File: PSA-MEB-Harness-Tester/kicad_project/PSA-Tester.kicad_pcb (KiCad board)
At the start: 4 copper layers, 100 x 100 mm, 41 parts, among them J11 TYPE-C-31-M-04, M1 MountingHole_3.2mm_M3_Pad_Via, M2 MountingHole_3.2mm_M3_Pad_Via, M3 MountingHole_3.2mm_M3_Pad_Via, M4 MountingHole_3.2mm_M3_Pad_Via, SW1 B3FS-1010P, SW2 B3FS-1010P, SW3 B3FS-1010P, U1 MCP23017T-E/SO, U10 ESP32-C3-OLED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

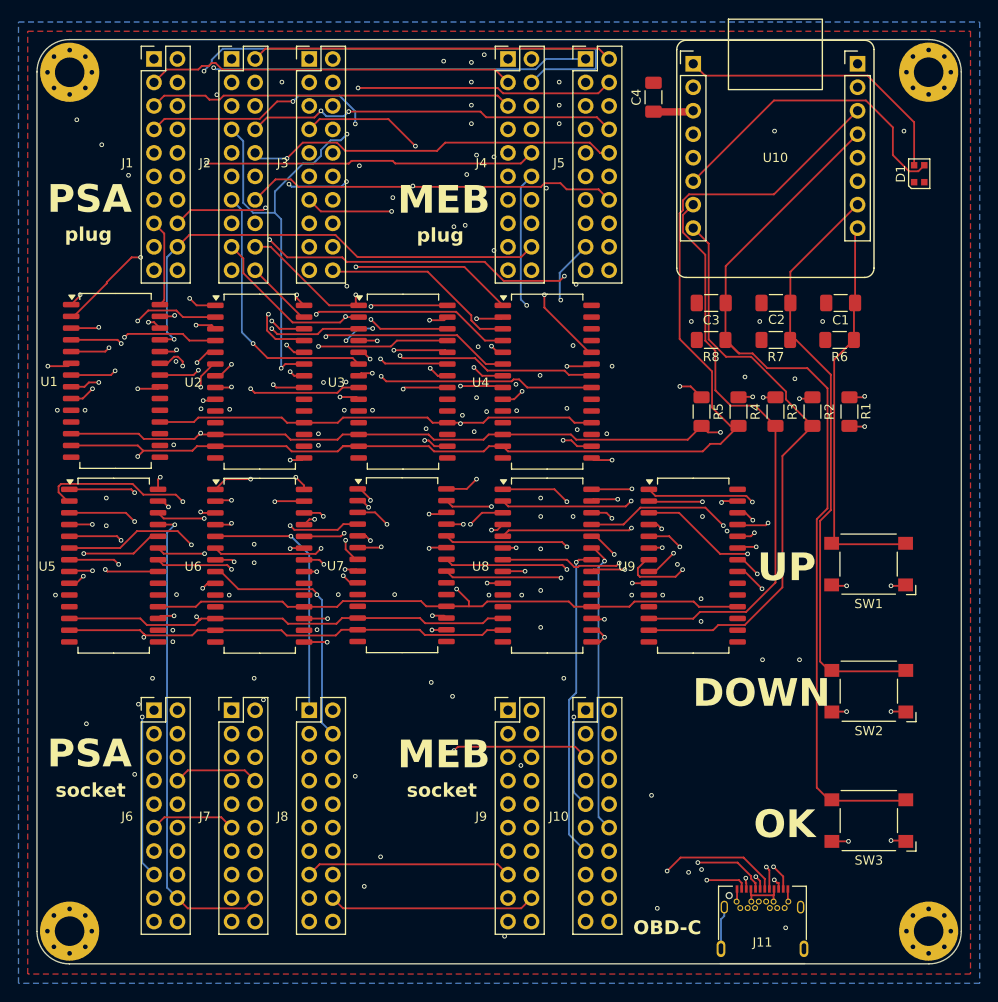
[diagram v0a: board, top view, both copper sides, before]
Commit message: fix PSA-Tester swapped pin headers
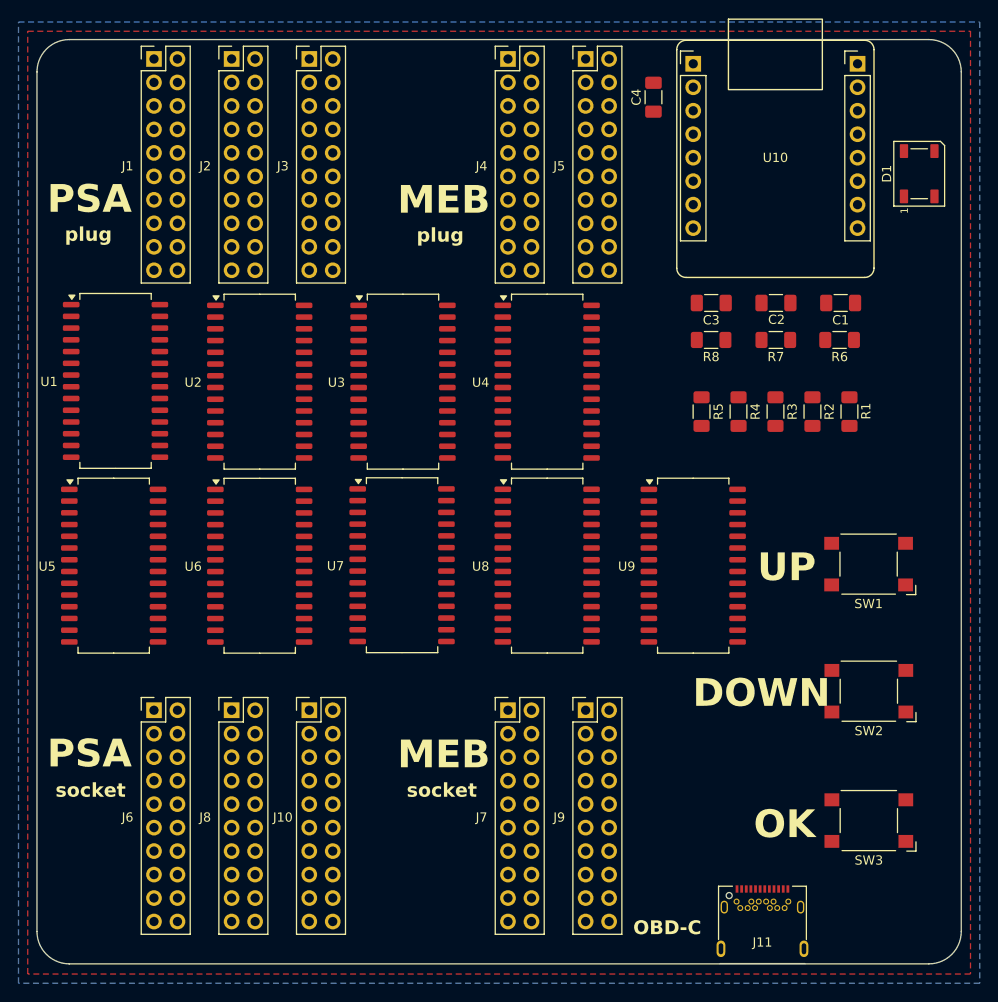
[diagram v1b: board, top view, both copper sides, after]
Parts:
- removed M1, M2, M3, M4: MountingHole_3.2mm_M3_Pad_Via, MountingHole:MountingHole_3.2mm_M3_Pad_Via
- D1: value XL-0807RGBC-WS2812B -> WS2812; footprint 0_tester:LED_WS2812B-2020_PLCC4_2.0x2.0mm -> LED_SMD:LED_WS2812B_PLCC4_5.0x5.0mm_P3.2mm
- J1, J10, J2, J3, J4, J5, J6, J7, J8, J9: footprint Connector_PinHeader_2.54mm:PinHeader_2x10_P2.54mm_Vertical -> 0_tester:PinHeader_2x10_P2.54mm_Vertical
- moved J10 29.9 mm to (68.5, 115.5)
- moved J7 29.9 mm to (90.0, 115.5)
- moved J9 8.40 mm to (98.4, 115.5)
- moved J8 8.40 mm to (60.1, 115.5)
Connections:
- J1 pad 11: 20 -> 11
- J1 pad 12: 19 -> 12
- J1 pad 13: 18 -> 13
- J1 pad 14: 17 -> 14
- J1 pad 15: 16 -> 15
- J1 pad 16: 15 -> 16
- J1 pad 17: 14 -> 17
- J1 pad 18: 13 -> 18
- J1 pad 19: 12 -> 19
- J1 pad 20: 11 -> 20
- J10 pad 11: 60a -> 51a
- J10 pad 12: 59a -> 52a
- J10 pad 13: 58a -> 53a
- J10 pad 14: 57a -> 54a
- J10 pad 15: 56a -> 55a
- J10 pad 16: 55a -> 56a
- J10 pad 17: 54a -> 57a
- J10 pad 18: 53a -> 58a
- J10 pad 19: 52a -> 59a
- J10 pad 20: 51a -> 60a
- J2 pad 11: 40 -> 31
- J2 pad 12: 39 -> 32
- J2 pad 13: 38 -> 33
- J2 pad 14: 37 -> 34
- J2 pad 15: 36 -> 35
- J2 pad 16: 35 -> 36
- J2 pad 17: 34 -> 37
- J2 pad 18: 33 -> 38
- J2 pad 19: 32 -> 39
- J2 pad 20: 31 -> 40
- J3 pad 11: 60 -> 51
- J3 pad 12: 59 -> 52
- J3 pad 13: 58 -> 53
- J3 pad 14: 57 -> 54
- J3 pad 15: 56 -> 55
- J3 pad 16: 55 -> 56
- J3 pad 17: 54 -> 57
- J3 pad 18: 53 -> 58
- J3 pad 19: 52 -> 59
- J3 pad 20: 51 -> 60
- J4 pad 11: 20 -> 11
- J4 pad 12: 19 -> 12
- J4 pad 13: 18 -> 13
- J4 pad 14: 17 -> 14
- J4 pad 15: 16 -> 15
- J4 pad 16: 15 -> 16
- J4 pad 17: 14 -> 17
- J4 pad 18: 13 -> 18
- J4 pad 19: 12 -> 19
- J4 pad 20: 11 -> 20
- J5 pad 11: 40 -> 31
- J5 pad 12: 39 -> 32
- J5 pad 13: 38 -> 33
- J5 pad 14: 37 -> 34
- J5 pad 15: 36 -> 35
- J5 pad 16: 35 -> 36
- J5 pad 17: 34 -> 37
- J5 pad 18: 33 -> 38
- J5 pad 19: 32 -> 39
- J5 pad 20: 31 -> 40
- J6 pad 11: 20a -> 11a
- J6 pad 12: 19a -> 12a
- J6 pad 13: 18a -> 13a
- J6 pad 14: 17a -> 14a
- J6 pad 15: 16a -> 15a
- J6 pad 16: 15a -> 16a
- J6 pad 17: 14a -> 17a
- J6 pad 18: 13a -> 18a
- J6 pad 19: 12a -> 19a
- J6 pad 20: 11a -> 20a
- J7 pad 1: 1a -> 21a
- J7 pad 10: 10a -> 30a
- J7 pad 11: 20a -> 31a
- J7 pad 12: 19a -> 32a
- J7 pad 13: 18a -> 33a
- J7 pad 14: 17a -> 34a
- J7 pad 15: 16a -> 35a
- J7 pad 16: 15a -> 36a
- J7 pad 17: 14a -> 37a
- J7 pad 18: 13a -> 38a
- J7 pad 19: 12a -> 39a
- J7 pad 2: 2a -> 22a
- J7 pad 20: 11a -> 40a
- J7 pad 3: 3a -> 23a
- J7 pad 4: 4a -> 24a
- J7 pad 5: 5a -> 25a
- J7 pad 6: 6a -> 26a
- J7 pad 7: 7a -> 27a
- J7 pad 8: 8a -> 28a
- J7 pad 9: 9a -> 29a
- J8 pad 1: 21a -> 1a
- J8 pad 10: 30a -> 10a
- J8 pad 11: 40a -> 11a
- J8 pad 12: 39a -> 12a
- J8 pad 13: 38a -> 13a
- J8 pad 14: 37a -> 14a
- J8 pad 15: 36a -> 15a
- J8 pad 16: 35a -> 16a
- J8 pad 17: 34a -> 17a
- J8 pad 18: 33a -> 18a
- J8 pad 19: 32a -> 19a
- J8 pad 2: 22a -> 2a
- J8 pad 20: 31a -> 20a
- J8 pad 3: 23a -> 3a
- J8 pad 4: 24a -> 4a
- J8 pad 5: 25a -> 5a
- J8 pad 6: 26a -> 6a
- J8 pad 7: 27a -> 7a
- J8 pad 8: 28a -> 8a
- J8 pad 9: 29a -> 9a
- J9 pad 11: 40a -> 31a
- J9 pad 12: 39a -> 32a
- J9 pad 13: 38a -> 33a
- J9 pad 14: 37a -> 34a
- J9 pad 15: 36a -> 35a
- J9 pad 16: 35a -> 36a
- J9 pad 17: 34a -> 37a
- J9 pad 18: 33a -> 38a
- J9 pad 19: 32a -> 39a
- J9 pad 20: 31a -> 40a
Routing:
- net nRESET: track 217.0 -> 0.00 mm, vias 3 -> 0
- net SDA1: track 196.6 -> 0.00 mm, vias 2 -> 0
- net SCL1: track 185.6 -> 0.00 mm, vias 3 -> 0
- net 8: track 117.3 -> 0.00 mm, vias 3 -> 0
- net 9: track 99.8 -> 0.00 mm, vias 2 -> 0
- net 40: track 97.3 -> 0.00 mm, vias 2 -> 0
- net BUTTON3: track 97.0 -> 0.00 mm
- net 4: track 93.5 -> 0.00 mm, vias 2 -> 0
- net 26: track 93.1 -> 0.00 mm, vias 2 -> 0
- net 38: track 87.9 -> 0.00 mm, vias 2 -> 0
- net 17: track 85.2 -> 0.00 mm, vias 2 -> 0
- net 24: track 82.4 -> 0.00 mm, vias 3 -> 0
- net 6: track 82.2 -> 0.00 mm, vias 2 -> 0
- net 22: track 81.5 -> 0.00 mm, vias 1 -> 0
- net 21: track 78.5 -> 0.00 mm, vias 2 -> 0
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
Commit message: swap switches, move sockets 4mm right
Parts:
- added REF**: MountingHole_3.2mm_M3_Pad_Via, MountingHole:MountingHole_3.2mm_M3_Pad_Via, F.Cu at (135.5, 46.4)
- added REF**: MountingHole_3.2mm_M3_Pad_Via, MountingHole:MountingHole_3.2mm_M3_Pad_Via, F.Cu at (42.5, 139.4)
- added REF**: MountingHole_3.2mm_M3_Pad_Via, MountingHole:MountingHole_3.2mm_M3_Pad_Via, F.Cu at (42.5, 46.4)
- added REF**: MountingHole_3.2mm_M3_Pad_Via, MountingHole:MountingHole_3.2mm_M3_Pad_Via, F.Cu at (135.5, 139.4)
- D1: value WS2812 -> XL-0807RGBC-WS2812B; footprint LED_SMD:LED_WS2812B_PLCC4_5.0x5.0mm_P3.2mm -> 0_tester:LED_WS2812B-2020_PLCC4_2.0x2.0mm
- SW1, SW2, SW3: value B3FS-1010P -> TS-1057S-03126
- moved J10 4.07 mm to (72.5, 115.0)
- moved J6 4.07 mm to (55.7, 115.0)
- moved J7 4.07 mm to (94.0, 115.0)
- moved J9 4.07 mm to (102.4, 115.0)
- moved J8 4.07 mm to (64.1, 115.0)
- moved J11 4.04 mm to (121.5, 139.9)
- moved SW3 3.55 mm to (129.0, 123.8)
- moved SW1 3.10 mm to (129.0, 102.8)

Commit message: PSA-Tester partly routed
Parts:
- renumbered REF** to REF1, REF** to REF2, REF** to REF3, REF** to REF4
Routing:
- net nRESET: track 0.00 -> 198.2 mm, vias 0 -> 3
- net SDA1: track 0.00 -> 188.1 mm
- net SCL1: track 0.00 -> 186.9 mm
- net BUTTON3: track 0.00 -> 92.5 mm
- net BUTTON2: track 0.00 -> 65.1 mm
- net SDA2: track 0.00 -> 61.2 mm, vias 0 -> 1
- net SCL2: track 0.00 -> 59.8 mm, vias 0 -> 1
- net +3V3: track 0.00 -> 54.5 mm, vias 0 -> 28
- net BUTTON1: track 0.00 -> 46.4 mm
- net Net-(D1-DIN): track 0.00 -> 42.0 mm
- net +5V: track 0.00 -> 35.2 mm

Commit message: add GND vias
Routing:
- net nRESET: track 198.2 -> 214.3 mm, vias 3 -> 5
- net GND: vias 0 -> 48

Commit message: add usb-c routing
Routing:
- net 79: track 0.00 -> 18.3 mm
- net 78: track 0.00 -> 8.30 mm
- net 61: track 0.00 -> 2.92 mm
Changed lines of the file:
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@@
+	)
+	(segment
+		(start 122.17273 135.574)
+		(end 122.73 136.13127)
+		(width 0.2)
+		(layer "B.Cu")
+		(net 126)
+	)
+	(segment
+		(start 122.73 136.13127)
+		(end 122.73 136.16)
+		(width 0.2)
+		(layer "B.Cu")
+		(net 126)
+	)
+	(segment
+		(start 120.88727 135.574)
+		(end 122.17273 135.574)
+		(width 0.2)
+		(layer "B.Cu")
+		(net 126)
+	)
+	(segment
+		(start 120.33 136.13127)
+		(end 120.88727 135.574)
+		(width 0.2)
+		(layer "B.Cu")
+		(net 126)
+	)
+	(segment
+		(start 120.33 136.16)
+		(end 120.33 136.13127)
+		(width 0.2)
+		(layer "B.Cu")
+		(net 126)
+	)
+	(segment
+		(start 118.544 136.346)
+		(end 118.544 137.10273)
+		(width 0.2)
+		(layer "B.Cu")
+		(net 131)
+	)
+	(segment
+		(start 124.17273 137.446)
+		(end 124.516 137.10273)
+		(width 0.2)
+		(layer "B.Cu")
+		(net 131)
+	)
+	(segment
+		(start 124.516 137.10273)
+		(end 124.516 136.346)
+		(width 0.2)
+		(layer "B.Cu")
+		(net 131)
+	)
+	(segment
+		(start 118.544 137.10273)
+		(end 118.88727 137.446)
+		(width 0.2)
+		(layer "B.Cu")
+		(net 131)
+	)
+	(segment
+		(start 118.73 136.16)
+		(end 118.544 136.346)
+		(width 0.2)
+		(layer "B.Cu")
+		(net 131)
+	)
+	(segment
+		(start 118.88727 137.446)
+		(end 124.17273 137.446)
+		(width 0.2)
+		(layer "B.Cu")
+		(net 131)
+	)
+	(segment
+		(start 124.516 136.346)
+		(end 124.33 136.16)
+		(width 0.2)
+		(layer "B.Cu")
+		(net 131)
+	)
+	(segment
+		(start 117.4 136.76)
+		(end 117.4 140.91)
+		(width 0.2)
+		(layer "B.Cu")
+		(net 134)
+	)
+	(segment
+		(start 117.04 141.27)
+		(end 126.02 141.27)
+		(width 0.2)
+		(layer "B.Cu")
+		(net 134)
+	)
+	(segment
+		(start 125.66 140.91)
+		(end 126.02 141.27)
+		(width 0.2)
+		(layer "B.Cu")
+		(net 134)
+	)
+	(segment
+		(start 117.4 140.91)
+		(end 117.04 141.27)
+		(width 0.2)
+		(layer "B.Cu")
+		(net 134)
+	)
+	(segment
+		(start 125.66 136.76)
+		(end 125.66 140.91)
+		(width 0.2)
+		(layer "B.Cu")
+		(net 134)
 	)
 	(segment

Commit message: routed
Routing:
- net 5: track 0.00 -> 103.0 mm, vias 0 -> 4
- net 31: track 0.00 -> 99.9 mm, vias 0 -> 3
- net 24: track 0.00 -> 98.8 mm, vias 0 -> 3
- net 7: track 0.00 -> 87.8 mm, vias 0 -> 4
- net 26: track 0.00 -> 83.5 mm, vias 0 -> 2
- net 23a: track 0.00 -> 80.1 mm, vias 0 -> 2
- net 30a: track 0.00 -> 78.2 mm, vias 0 -> 2
- net 27: track 0.00 -> 77.1 mm, vias 0 -> 2
- net 34: track 0.00 -> 77.0 mm, vias 0 -> 3
- net 13: track 0.00 -> 76.6 mm, vias 0 -> 1
- net 12: track 0.00 -> 75.7 mm, vias 0 -> 1
- net 4: track 0.00 -> 74.5 mm, vias 0 -> 4
- net 11: track 0.00 -> 74.3 mm, vias 0 -> 1
- net 2: track 0.00 -> 74.2 mm, vias 0 -> 2
- net 1: track 0.00 -> 73.9 mm, vias 0 -> 2
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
